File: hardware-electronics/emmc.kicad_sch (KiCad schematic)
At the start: 42 parts, among them U2 EMMC16G-MW28-01E10, U4 24AA04T-I_OT, U8 USB2244-AEZG-06, Y2 ECS-240-10-47-CKM-TR

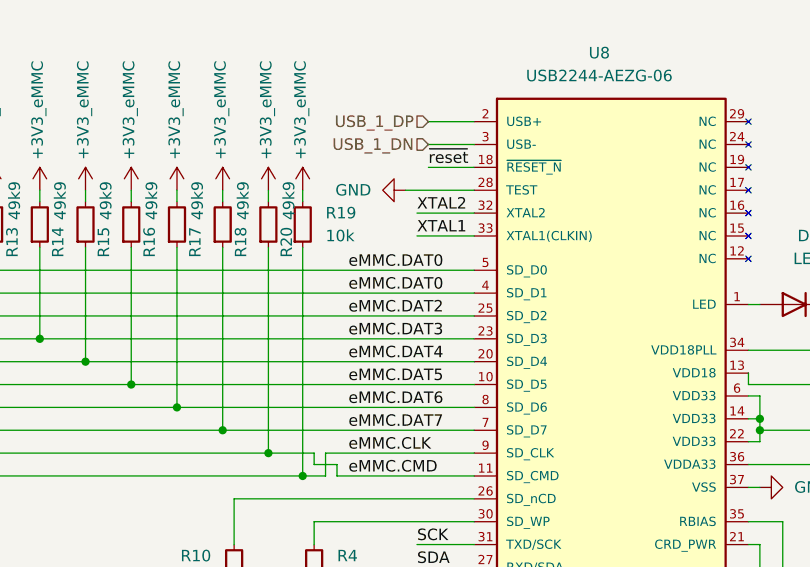
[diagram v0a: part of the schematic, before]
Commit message: [#20] PCB fix unconnected items
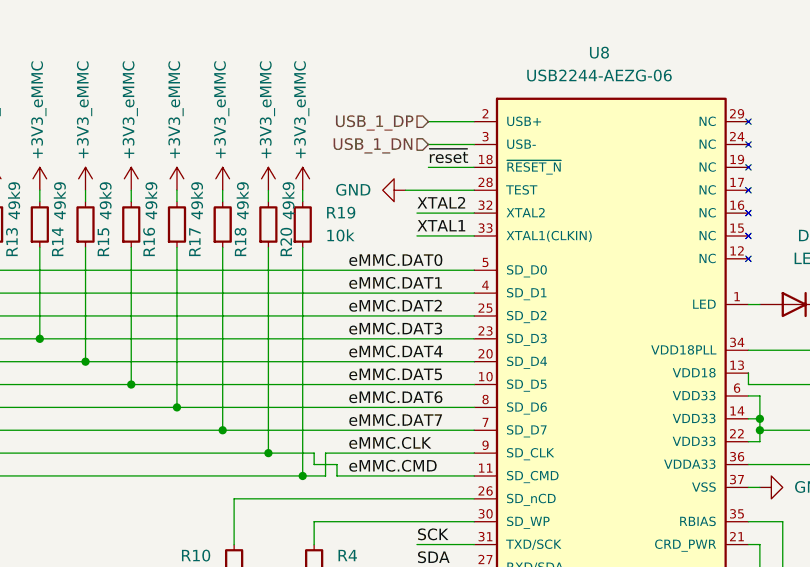
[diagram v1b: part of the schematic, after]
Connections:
- net eMMC.DAT0: no longer R12.1, U2.A4 (DAT1), U8.4 (SD_D1)
- new net eMMC.DAT1: R12.1, U2.A4 (DAT1), U8.4 (SD_D1)
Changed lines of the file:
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@@
 		)
 	)
-	(label "eMMC.DAT0"
+	(label "eMMC.DAT1"
 		(at 139.7 78.74 0)
 		(fields_autoplaced yes)

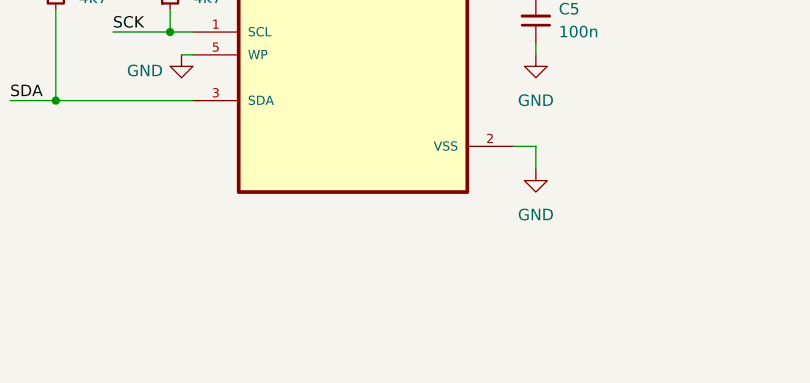
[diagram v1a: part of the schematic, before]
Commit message: [#24] PCB tag-connect programming connectors brainstorming
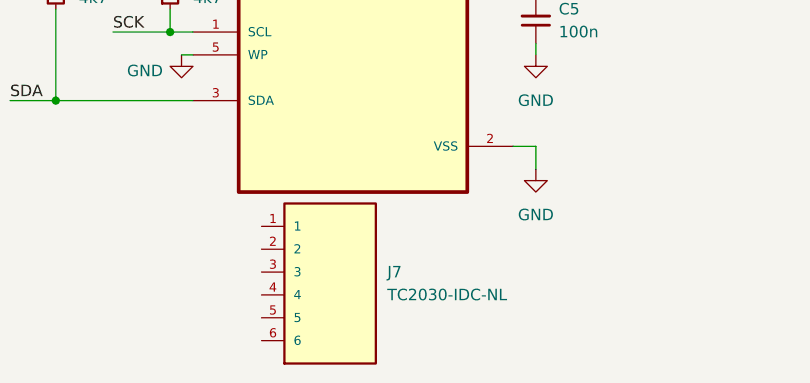
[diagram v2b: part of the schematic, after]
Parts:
- added J7: TC2030-IDC-NL, M2SmartHomeFootprints:TAG_TC2030-IDC-NL, symbol M2SmartHomeSymbols:TC2030-IDC-NL
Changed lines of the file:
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@@
+	)
+	(symbol
+		(lib_id "M2SmartHomeSymbols:TC2030-IDC-NL")
+		(at 137.16 190.5 0)
+		(unit 1)
+		(exclude_from_sim no)
+		(in_bom yes)
+		(on_board yes)
+		(dnp no)
+		(fields_autoplaced yes)
+		(property "Reference" "J7"
+			(at 143.51 187.9599 0)
+			(effects
+				(font
+					(size 1.27 1.27)
+				)
+				(justify left)
+			)
+		)
+		(property "Value" "TC2030-IDC-NL"
+			(at 143.51 190.4999 0)
+			(effects
+				(font
+					(size 1.27 1.27)
+				)
+				(justify left)
+			)
+		)
+		(property "Footprint" "M2SmartHomeFootprints:TAG_TC2030-IDC-NL"
+			(at 137.16 190.5 0)
+			(effects
+				(font
+					(size 1.27 1.27)
+				)
+				(justify bottom)
+				(hide yes)
+			)
+		)
+		(property "Datasheet" ""
+			(at 137.16 190.5 0)
+			(effects
+				(font
+					(size 1.27 1.27)
+				)
+				(hide yes)
+			)
+		)
+		(property "Description" ""
+			(at 137.16 190.5 0)
+			(effects
+				(font
+					(size 1.27 1.27)
+				)
+				(hide yes)
+			)
+		)
+		(property "MF" "Tag-Connect"
+			(at 137.16 190.5 0)
+			(effects
+				(font
+					(size 1.27 1.27)
+				)
+				(justify bottom)
+				(hide yes)
+			)
+		)
+		(property "Description_1" "\n                        \n                            PLUG-OF-NAILS 6-PIN W/O LEGS 8\n                        \n"
+			(at 137.16 190.5 0)
+			(effects
+				(font
+					(size 1.27 1.27)
+				)
+				(justify bottom)
+				(hide yes)
+			)
+		)
+		(property "Package" "None"
+			(at 137.16 190.5 0)
+			(effects
+				(font
+					(size 1.27 1.27)
+				)
+				(justify bottom)
+				(hide yes)
+			)
+		)
+		(property "Price" "None"
+			(at 137.16 190.5 0)
+			(effects
+				(font
+					(size 1.27 1.27)
+				)
+				(justify bottom)
+				(hide yes)
+			)
+		)
+		(property "Check_prices" "https://www.snapeda.com/parts/TC2030-IDC-NL/Tag-Connect/view-part/?ref=eda"
+			(at 137.16 190.5 0)
+			(effects
+				(font
+					(size 1.27 1.27)
+				)
+				(justify bottom)
+				(hide yes)
+			)
+		)
+		(property "STANDARD" "Manufacturer recommendation"
+			(at 137.16 190.5 0)
+			(effects
+				(font
+					(size 1.27 1.27)
+				)
+				(justify bottom)
+				(hide yes)
+			)
+		)
+		(property "PARTREV" "MS"
+			(at 137.16 190.5 0)
+			(effects
+				(font
+					(size 1.27 1.27)
+				)
+				(justify bottom)
+				(hide yes)
+			)
+		)
+		(property "SnapEDA_Link" "https://www.snapeda.com/parts/TC2030-IDC-NL/Tag-Connect/view-part/?ref=snap"
+			(at 137.16 190.5 0)
+			(effects
+				(font
+					(size 1.27 1.27)
+				)
+				(justify bottom)
+				(hide yes)
+			)
+		)
+		(property "MP" "TC2030-IDC-NL"
+			(at 137.16 190.5 0)
+			(effects
+				(font
+					(size 1.27 1.27)
+				)
+				(justify bottom)
+				(hide yes)
+			)
+		)
+		(property "Availability" "Not in stock"
+			(at 137.16 190.5 0)
+			(effects
+				(font
+					(size 1.27 1.27)
+				)
+				(justify bottom)
+				(hide yes)
+			)
+		)
+		(property "MANUFACTURER" "Tag-Connect"
+			(at 137.16 190.5 0)
+			(effects
+				(font
+					(size 1.27 1.27)
+				)
+				(justify bottom)
+				(hide yes)
+			)
+		)
+		(pin "6"
+		)
+		(pin "2"
+		)
+		(pin "5"
+		)
+		(pin "4"
+		)
+		(pin "3"
+		)
+		(pin "1"
+		)
+		(instances
+			(project "M2SmartHome"
+				(path "/da663dec-9e91-4003-a791-431d460ad63c/d6ad415e-1295-4f8b-8193-bff1569600a2"
+					(reference "J7")
+					(unit 1)
+				)
+			)
+		)
 	)
 	(symbol

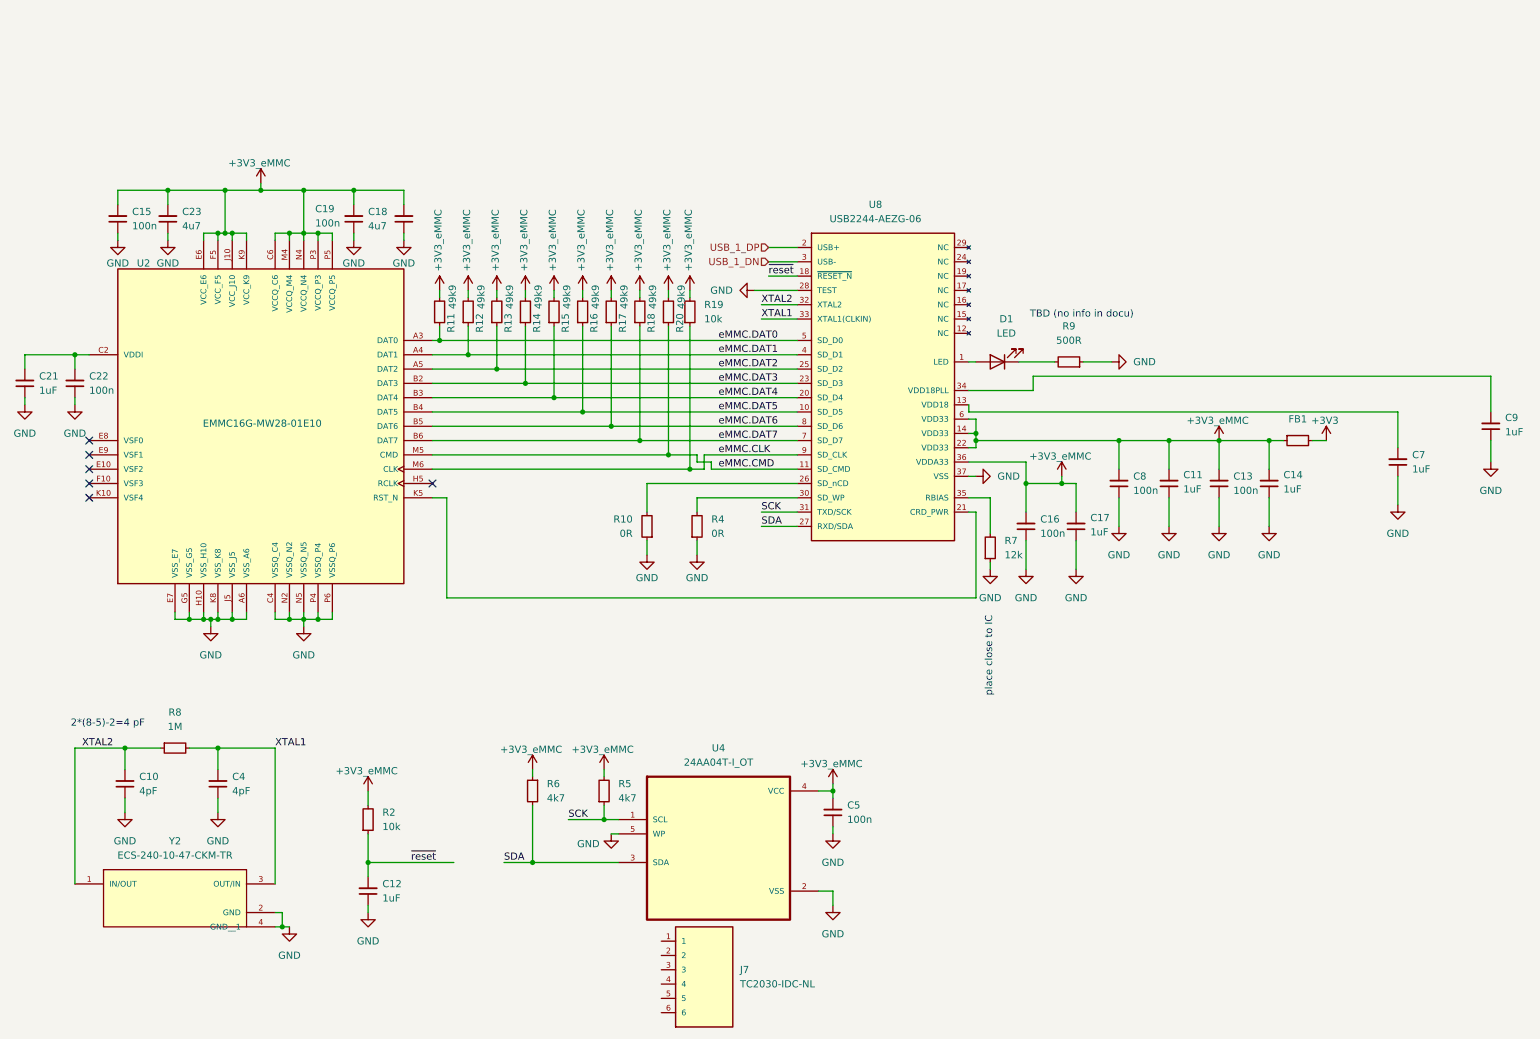
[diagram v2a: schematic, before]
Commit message: [#26] Remove power plane splits for invidual devices
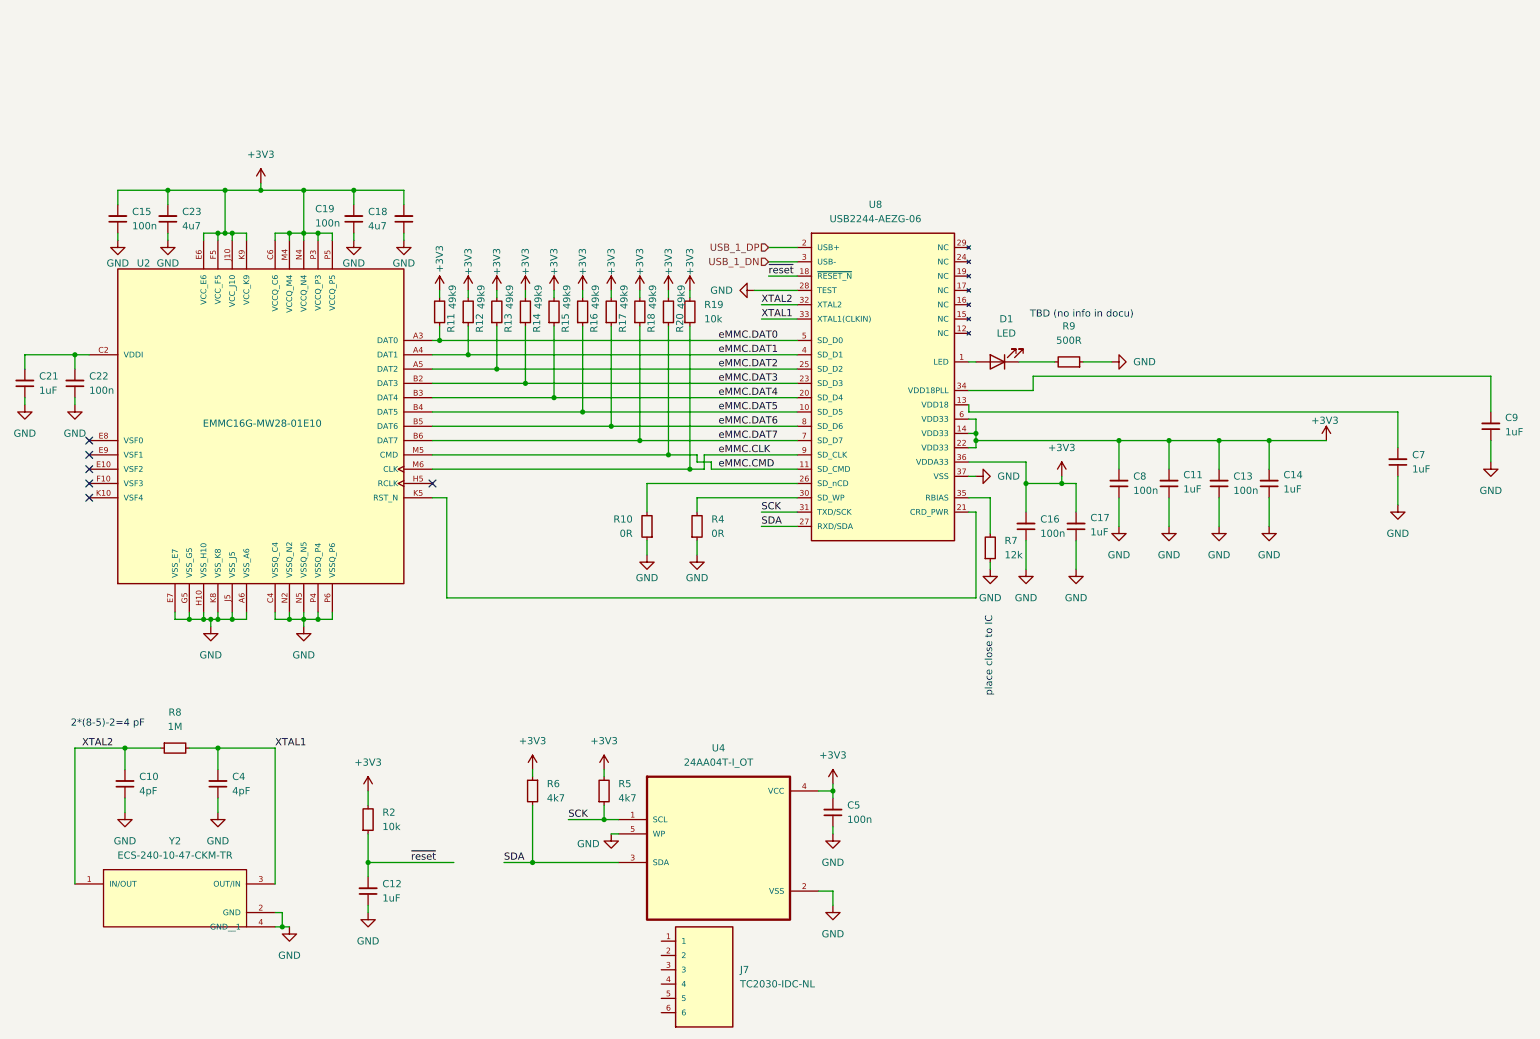
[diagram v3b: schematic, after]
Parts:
- removed FB1: FB_120R_0603, M2SmartHomeFootprints:FB_0603, symbol M2SmartHomeSymbols:FB_120R_0603
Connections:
- net +3V3_eMMC is gone; now on net +3V3: C11.2, C13.2, C14.2, C15.2, C16.2, C17.2, C18.2, C19.2, C23.2, C5.2, C8.2, R11.2, R12.2, R13.2, R14.2, R15.2, R16.2, R17.2, R18.2, R19.2, R2.2, R20.2, R5.2, R6.1, U2.C6 (VCCQ_C6), U2.E6 (VCC_E6), U2.F5 (VCC_F5), U2.J10 (VCC_J10), U2.K9 (VCC_K9), U2.M4 (VCCQ_M4), U2.N4 (VCCQ_N4), U2.P3 (VCCQ_P3), U2.P5 (VCCQ_P5), U4.4 (VCC), U8.14 (VDD33), U8.22 (VDD33), U8.36 (VDDA33), U8.6 (VDD33)

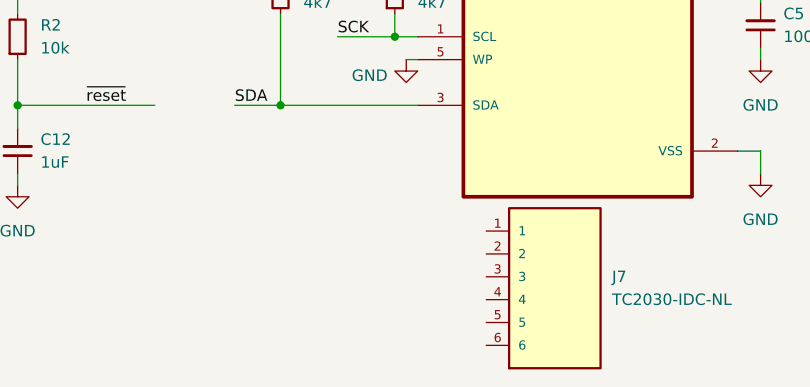
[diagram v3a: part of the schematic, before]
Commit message: [#26] Add programing interface for I2c devices
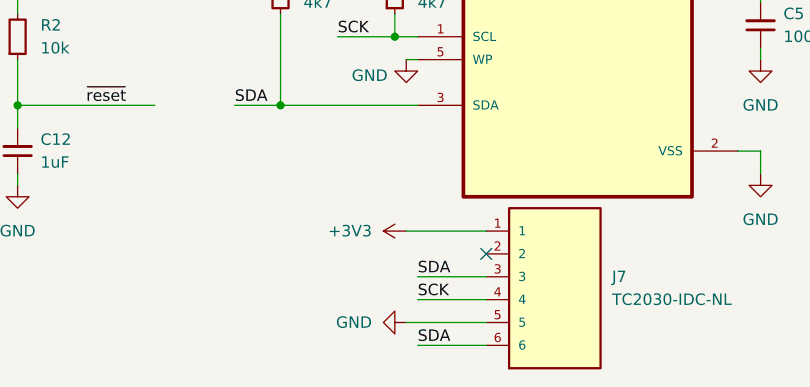
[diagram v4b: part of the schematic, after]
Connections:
- net +3V3: now also J7.1
- net GND: now also J7.5
- net SCK: now also J7.4
- net SDA: now also J7.3, J7.6
- no-connect marks 6 -> 7
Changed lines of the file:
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@@
 		(at 88.9 101.6)
 	)
+	(no_connect
+		(at 129.54 185.42)
+	)
 	(wire
 		(pts
@@
 	(wire
 		(pts
+			(xy 120.65 182.88) (xy 129.54 182.88)
+		)
+		(stroke
+			(width 0)
+			(type default)
+		)
+	)
+	(wire
+		(pts
 			(xy 147.32 69.85) (xy 153.67 69.85)
 		)
@@
 	(wire
 		(pts
+			(xy 121.92 187.96) (xy 129.54 187.96)
+		)
+		(stroke
+			(width 0)
+			(type default)
+		)
+	)
+	(wire
+		(pts
 			(xy 66.04 57.15) (xy 66.04 49.53)
 		)
@@
 	(wire
 		(pts
+			(xy 121.92 195.58) (xy 129.54 195.58)
+		)
+		(stroke
+			(width 0)
+			(type default)
+		)
+	)
+	(wire
+		(pts
 			(xy 25.4 86.36) (xy 25.4 87.63)
 		)
@@
 	(wire
 		(pts
+			(xy 120.65 193.04) (xy 129.54 193.04)
+		)
+		(stroke
+			(width 0)
+			(type default)
+		)
+	)
+	(wire
+		(pts
 			(xy 203.2 101.6) (xy 203.2 106.68)
 		)
@@
 	(wire
 		(pts
+			(xy 121.92 190.5) (xy 129.54 190.5)
+		)
+		(stroke
+			(width 0)
+			(type default)
+		)
+	)
+	(wire
+		(pts
 			(xy 219.71 93.98) (xy 228.6 93.98)
 		)
@@
 		)
 	)
+	(label "SDA"
+		(at 121.92 195.58 0)
+		(fields_autoplaced yes)
+		(effects
+			(font
+				(size 1.27 1.27)
+			)
+			(justify left bottom)
+		)
+	)
 	(label "eMMC.CLK"
 		(at 139.7 96.52 0)
@@
 		)
 	)
+	(label "SCK"
+		(at 121.92 190.5 0)
+		(fields_autoplaced yes)
+		(effects
+			(font
+				(size 1.27 1.27)
+			)
+			(justify left bottom)
+		)
+	)
 	(label "eMMC.DAT1"
 		(at 139.7 78.74 0)
@@
 		)
 	)
+	(label "SDA"
+		(at 121.92 187.96 0)
+		(fields_autoplaced yes)
+		(effects
+			(font
+				(size 1.27 1.27)
+			)
+			(justify left bottom)
+		)
+	)
 	(label "eMMC.DAT0"
 		(at 139.7 76.2 0)
@@
 	(symbol
 		(lib_id "power:+3V3")
+		(at 120.65 182.88 90)
+		(unit 1)
+		(exclude_from_sim no)
+		(in_bom yes)
+		(on_board yes)
+		(dnp no)
+		(fields_autoplaced yes)
+		(property "Reference" "#PWR0171"
+			(at 124.46 182.88 0)
+			(effects
+				(font
+					(size 1.27 1.27)
+				)
+				(hide yes)
+			)
+		)
+		(property "Value" "+3V3"
+			(at 116.84 182.8799 90)
+			(effects
+				(font
+					(size 1.27 1.27)
+				)
+				(justify left)
+			)
+		)
+		(property "Footprint" ""
+			(at 120.65 182.88 0)
+			(effects
+				(font
+					(size 1.27 1.27)
+				)
+				(hide yes)
+			)
+		)
+		(property "Datasheet" ""
+			(at 120.65 182.88 0)
+			(effects
+				(font
+					(size 1.27 1.27)
+				)
+				(hide yes)
+			)
+		)
+		(property "Description" "Power symbol creates a global label with name \"+3V3\""
+			(at 120.65 182.88 0)
+			(effects
+				(font
+					(size 1.27 1.27)
+				)
+				(hide yes)
+			)
+		)
+		(pin "1"
+		)
+		(instances
+			(project "M2SmartHome"
+				(path "/da663dec-9e91-4003-a791-431d460ad63c/d6ad415e-1295-4f8b-8193-bff1569600a2"
+					(reference "#PWR0171")
+					(unit 1)
+				)
+			)
+		)
+	)
+	(symbol
+		(lib_id "power:+3V3")
 		(at 119.38 152.4 0)
 		(unit 1)
@@
 					(unit 1)
 				)
+			)
+		)
+	)
+	(symbol
+		(lib_id "power:GND")
+		(at 120.65 193.04 270)
+		(unit 1)
+		(exclude_from_sim no)
+		(in_bom yes)
+		(on_board yes)
+		(dnp no)
+		(fields_autoplaced yes)
+		(property "Reference" "#PWR0172"
+			(at 114.3 193.04 0)
+			(effects
+				(font
+					(size 1.27 1.27)
+				)
+				(hide yes)
+			)
+		)
+		(property "Value" "GND"
+			(at 116.84 193.0399 90)
+			(effects
+				(font
+					(size 1.27 1.27)
+				)
+				(justify right)
+			)
+		)
+		(property "Footprint" ""
+			(at 120.65 193.04 0)
+			(effects
+				(font
+					(size 1.27 1.27)
+				)
+				(hide yes)
+			)
+		)
+		(property "Datasheet" ""
+			(at 120.65 193.04 0)
+			(effects
+				(font
+					(size 1.27 1.27)
+				)
+				(hide yes)
+			)
+		)
+		(property "Description" "Power symbol creates a global label with name \"GND\" , ground"
+			(at 120.65 193.04 0)
+			(effects
+				(font
+					(size 1.27 1.27)
+				)
+				(hide yes)
+			)
+		)
+		(pin "1"
+		)
+		(instances
+			(project "M2SmartHome"
+				(path "/da663dec-9e91-4003-a791-431d460ad63c/d6ad415e-1295-4f8b-8193-bff1569600a2"
+					(reference "#PWR0172")
+					(unit 1)
+				)

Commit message: [#26] Correct MPN GRM155R61A104KA01D
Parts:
- C13, C15, C16, C19, C22, C5, C8: Author Your Name -> Lukasz Nowarkiewicz; MPN GRM155R61A104KE01D -> GRM155R61A104KA01D
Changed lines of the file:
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@@
 			)
 		)
-		(property "MPN" "GRM155R61A104KE01D"
+		(property "MPN" "GRM155R61A104KA01D"
 			(at 92.71 36.83 0)
 			(effects
@@
 			)
 		)
-		(property "Author" "Your Name"
+		(property "Author" "Lukasz Nowarkiewicz"
 			(at 100.33 36.83 0)
 			(effects
@@
 			)
 		)
-		(property "MPN" "GRM155R61A104KE01D"
+		(property "MPN" "GRM155R61A104KA01D"
 			(at 50.8 36.83 0)
 			(effects
@@
 			)
 		)
-		(property "Author" "Your Name"
+		(property "Author" "Lukasz Nowarkiewicz"
 			(at 58.42 36.83 0)
 			(effects
@@
 			)
 		)
-		(property "MPN" "GRM155R61A104KE01D"
+		(property "MPN" "GRM155R61A104KA01D"
 			(at 177.8 142.24 0)
 			(effects
@@
 			)
 		)
-		(property "Author" "Your Name"
+		(property "Author" "Lukasz Nowarkiewicz"
 			(at 185.42 142.24 0)
 			(effects
@@
 			)
 		)
-		(property "MPN" "GRM155R61A104KE01D"
+		(property "MPN" "GRM155R61A104KA01D"
 			(at 228.6 83.82 0)
 			(effects
@@
 			)
 		)
-		(property "Author" "Your Name"
+		(property "Author" "Lukasz Nowarkiewicz"
 			(at 236.22 83.82 0)
 			(effects
@@
 			)
 		)
-		(property "MPN" "GRM155R61A104KE01D"
+		(property "MPN" "GRM155R61A104KA01D"
 			(at 212.09 91.44 0)
 			(effects
@@
 			)
 		)
-		(property "Author" "Your Name"
+		(property "Author" "Lukasz Nowarkiewicz"
 			(at 219.71 91.44 0)
 			(effects
@@
 			)
 		)
-		(property "MPN" "GRM155R61A104KE01D"
+		(property "MPN" "GRM155R61A104KA01D"
 			(at 43.18 66.04 0)
 			(effects
@@
 			)
 		)
-		(property "Author" "Your Name"
+		(property "Author" "Lukasz Nowarkiewicz"
 			(at 50.8 66.04 0)
 			(effects
@@
 			)
 		)
-		(property "MPN" "GRM155R61A104KE01D"
+		(property "MPN" "GRM155R61A104KA01D"
 			(at 246.38 83.82 0)
 			(effects
@@
 			)
 		)
-		(property "Author" "Your Name"
+		(property "Author" "Lukasz Nowarkiewicz"
 			(at 254 83.82 0)
 			(effects
